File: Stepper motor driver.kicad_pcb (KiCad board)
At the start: 2 copper layers, 16 parts, among them P1 CONN_01X04, P2 CONN_01X04, Q1 TIP120, Q2 TIP120, Q3 TIP120, Q4 TIP120, U1 74LS175, U2 74LS157

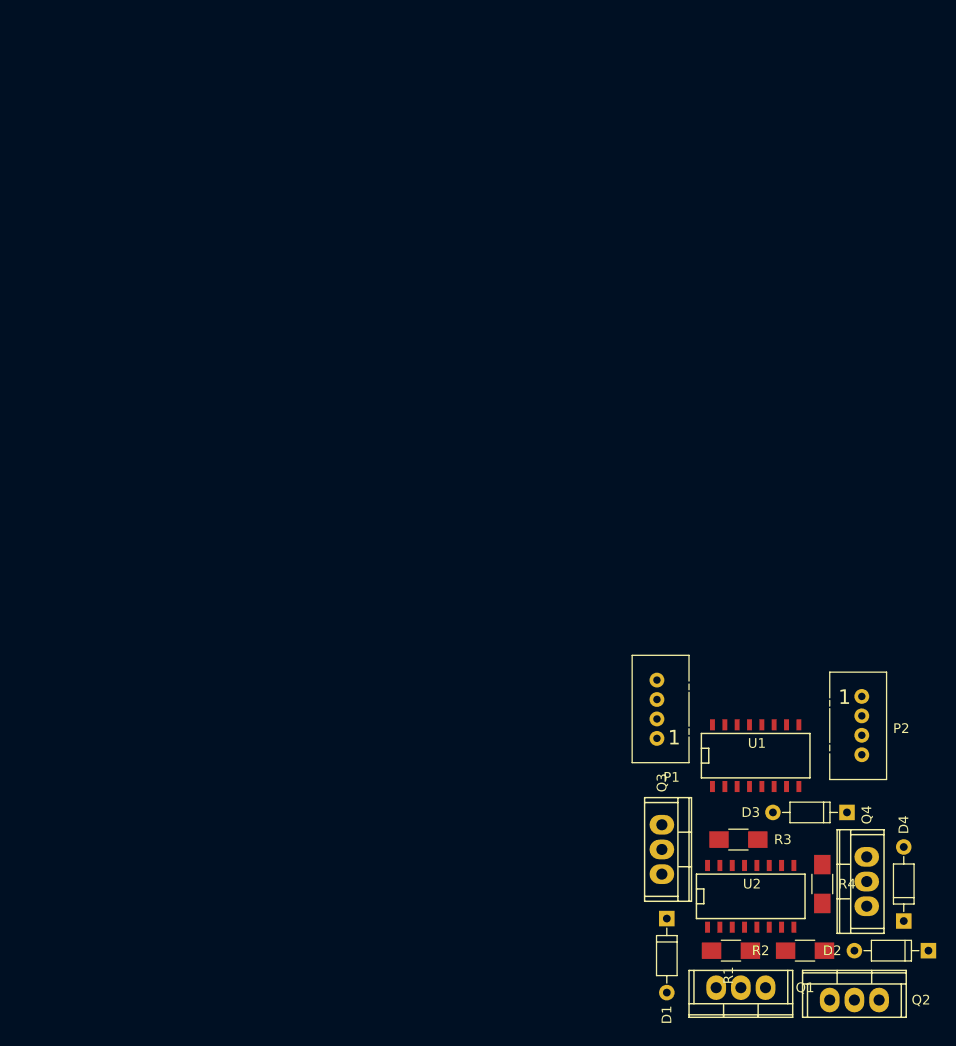
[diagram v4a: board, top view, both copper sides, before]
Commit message: Cleaned up schematic and placed PCB components
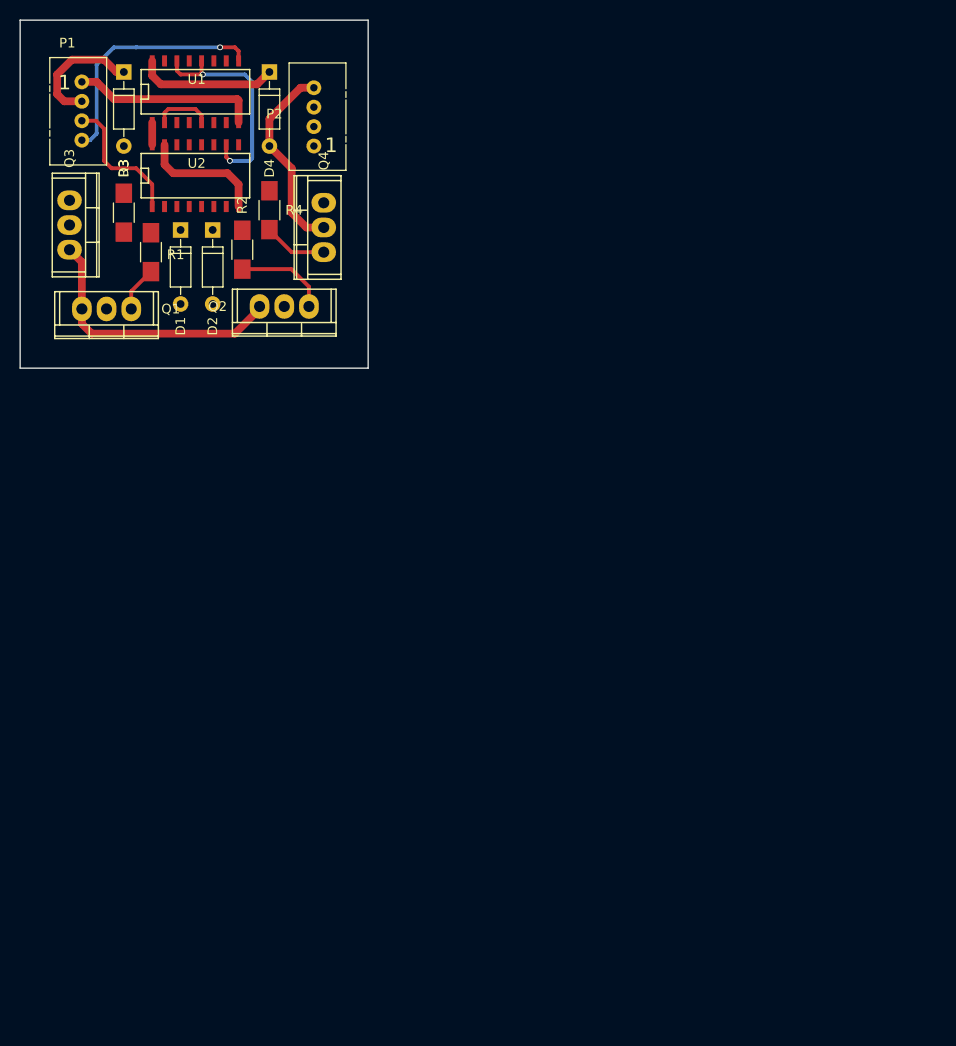
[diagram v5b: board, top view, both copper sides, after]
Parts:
- moved D4 109.1 mm to (144.0, 29.7), turned to 270 degrees
- moved D3 106.5 mm to (129.0, 29.7), turned to 270 degrees
- moved D2 104.5 mm to (138.2, 46.0), turned to 270 degrees
- moved Q1 95.6 mm to (127.3, 54.1)
- moved U2 93.6 mm to (136.4, 40.4)
- moved R1 93.4 mm to (131.8, 48.3), turned to 90 degrees
- moved R2 92.5 mm to (141.2, 48.0), turned to 90 degrees
- moved Q2 92.4 mm to (145.5, 53.8), turned to 180 degrees
- moved R3 90.3 mm to (129.0, 44.2), turned to 90 degrees
- moved P1 89.8 mm to (124.7, 30.7), turned to 0 degrees
- moved R4 89.7 mm to (144.0, 43.9)
- moved U1 89.4 mm to (136.4, 31.8)
- moved Q3 88.6 mm to (123.4, 45.5)
- moved Q4 87.5 mm to (149.6, 45.7)
- moved D1 86.8 mm to (134.9, 46.0)
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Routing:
- net GND: track 0.00 -> 60.1 mm
- net VCC: track 0.00 -> 29.7 mm
- net /CLK: track 0.00 -> 25.4 mm, vias 0 -> 1
- net /B2-: track 0.00 -> 22.8 mm, vias 0 -> 2
- net Net-(D4-Pad2): track 0.00 -> 20.4 mm
- net /DIR: track 0.00 -> 14.2 mm
- net Net-(Q2-Pad1): track 0.00 -> 9.64 mm
- net Net-(Q4-Pad1): track 0.00 -> 6.57 mm
- net /B1+: track 0.00 -> 6.01 mm
- net Net-(Q1-Pad1): track 0.00 -> 4.68 mm
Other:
- board outline added: 35.8 x 35.8 mm

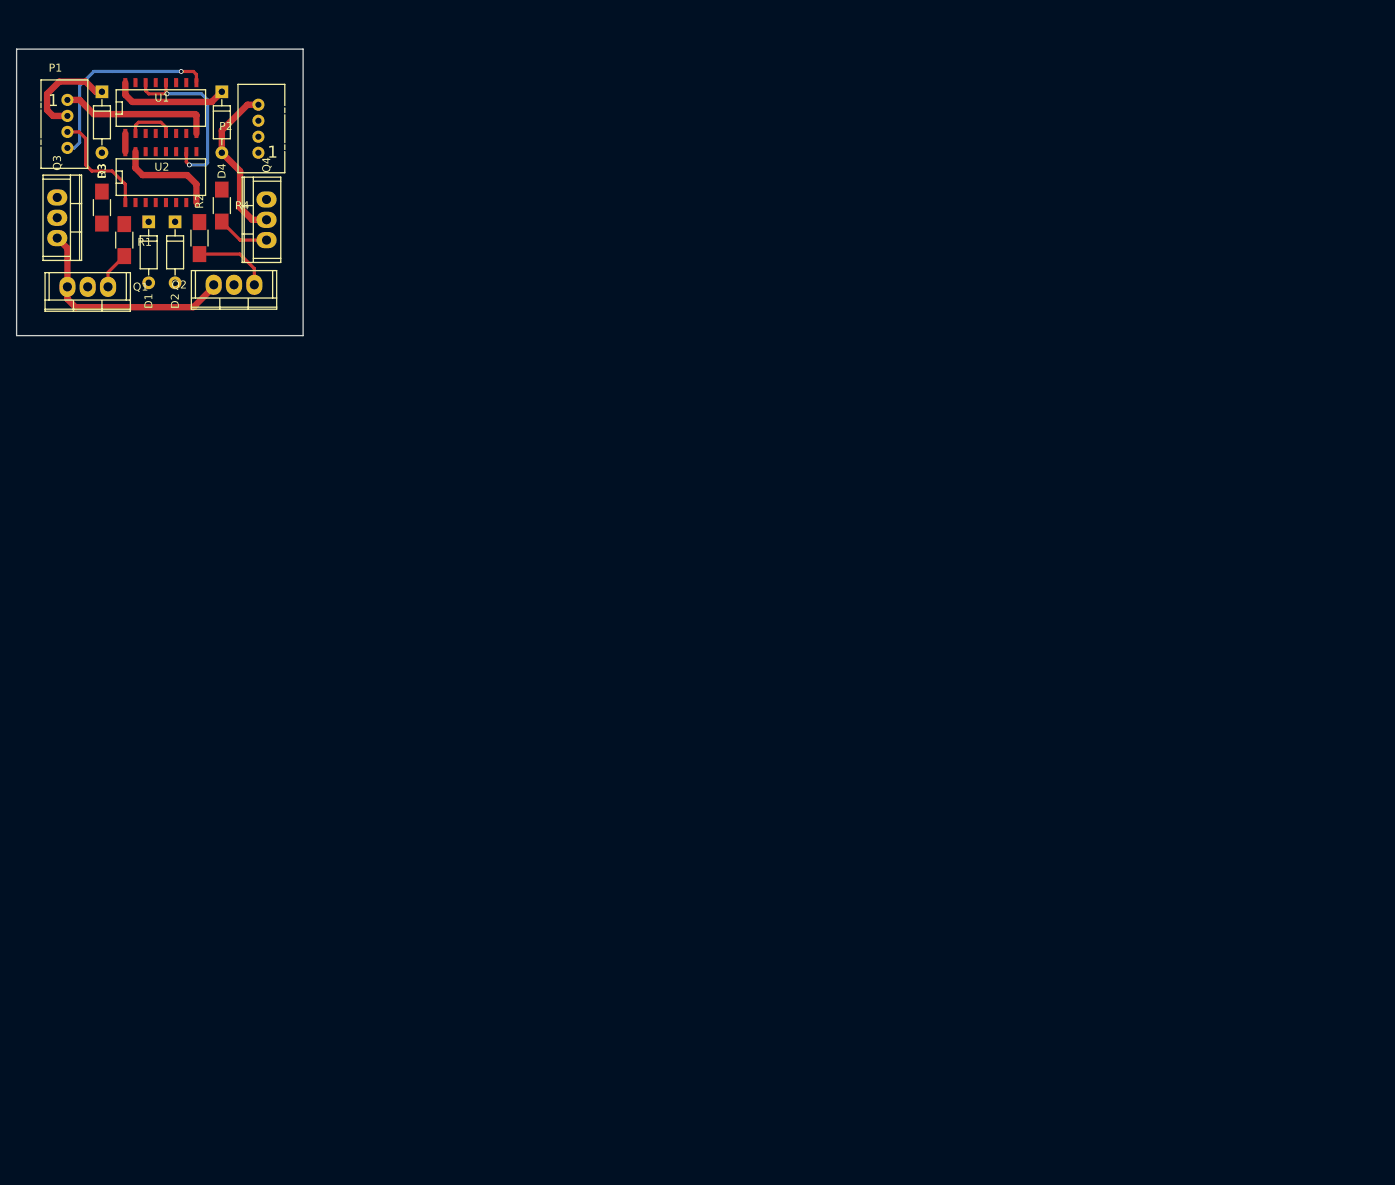
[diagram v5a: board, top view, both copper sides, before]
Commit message: Small schematic change, fine component placement, silkscreen
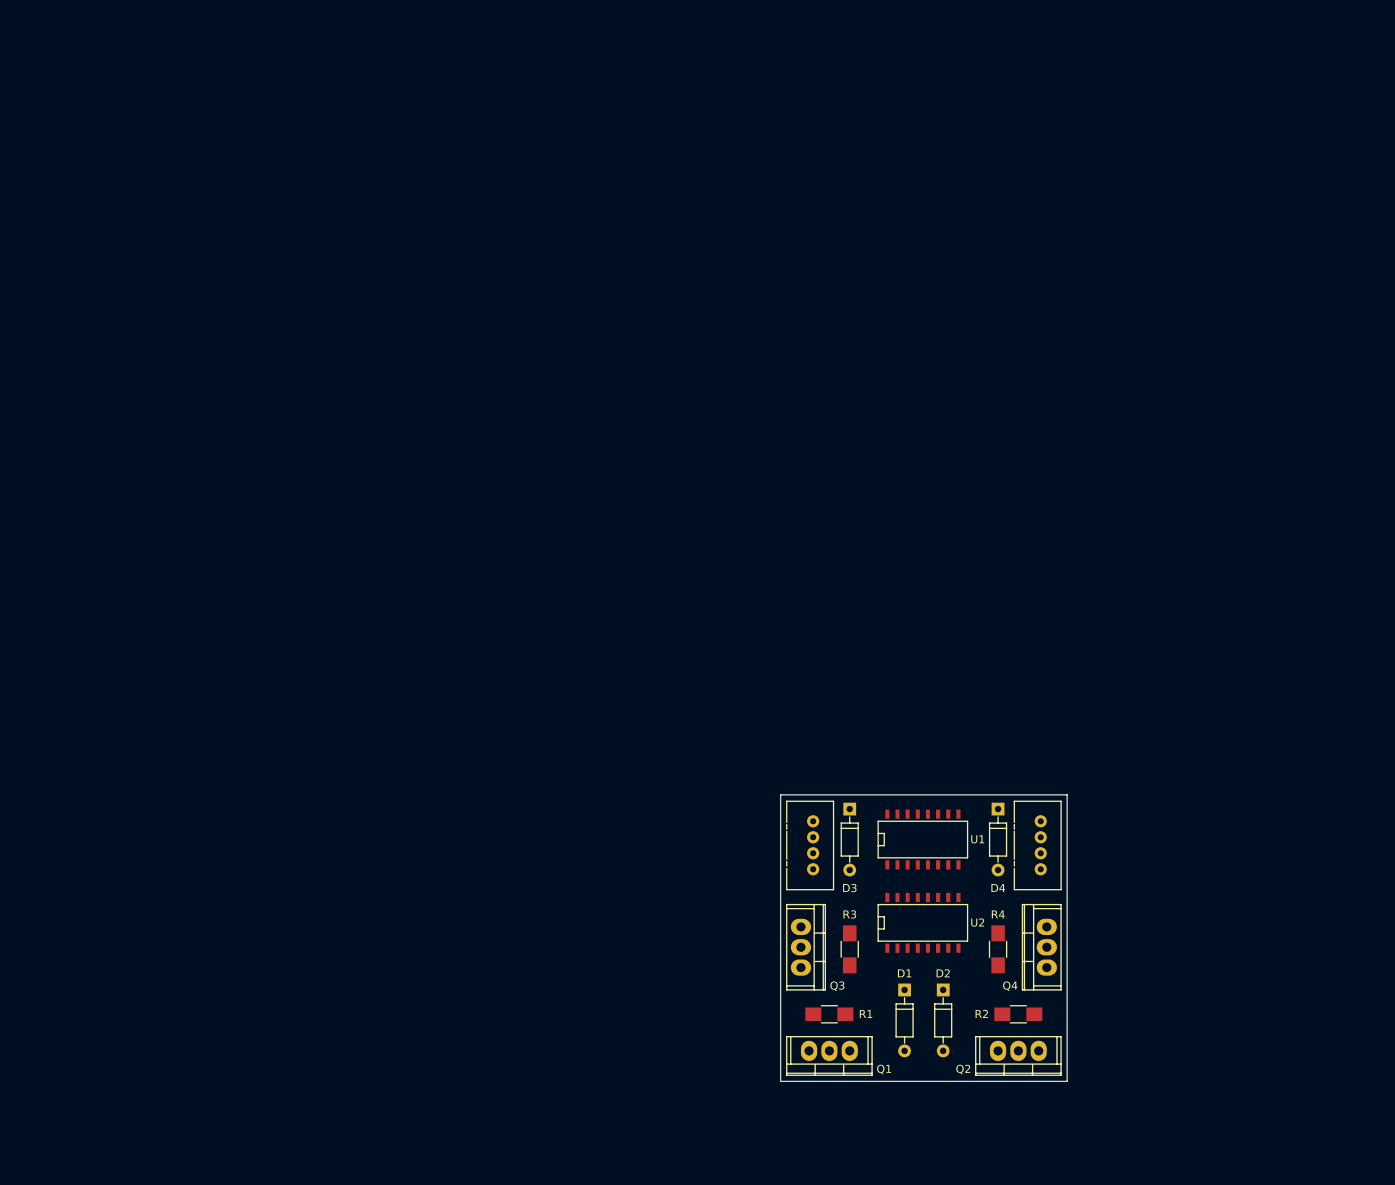
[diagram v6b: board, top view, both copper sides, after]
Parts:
- removed P1, P2: CONN_01X04, Connect:Grove_1x04
- added ?: CONN_01X04, Connect:Grove_1x04, F.Cu at (217.9, 120.9)
- added ?: CONN_01X04, Connect:Grove_1x04, F.Cu at (246.4, 120.9)
- moved R2 141.0 mm to (243.6, 145.0), turned to 180 degrees
- moved Q2 137.0 mm to (243.6, 149.6)
- moved D2 135.8 mm to (234.2, 142.0)
- moved D1 134.7 mm to (229.4, 142.0)
- moved R4 134.4 mm to (241.0, 136.9)
- moved Q4 133.3 mm to (247.1, 136.7)
- moved U2 133.3 mm to (231.6, 133.6)
- moved Q1 133.1 mm to (220.0, 149.6)
- moved D4 132.1 mm to (241.0, 119.4)
- moved U1 132.0 mm to (231.6, 123.2)
- moved R3 131.7 mm to (222.5, 136.9)
- moved R1 130.9 mm to (220.0, 145.0), turned to 0 degrees
- moved Q3 130.2 mm to (216.4, 136.7)
- moved D3 129.5 mm to (222.5, 119.4)
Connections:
- net Net-(D1-Pad2) renamed /Coil1+
- net Net-(D2-Pad2) renamed /Coil1-
- net Net-(D3-Pad2) renamed /Coil2+
- net Net-(D4-Pad2) renamed /Coil2-
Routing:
- net GND: track 60.1 -> 0.00 mm
- net VCC: track 29.7 -> 0.00 mm
- net /CLK: track 25.4 -> 0.00 mm, vias 1 -> 0
- net /B2-: track 22.8 -> 0.00 mm, vias 2 -> 0
- net /Coil2-: track 20.4 -> 0.00 mm
- net /DIR: track 14.2 -> 0.00 mm
- net Net-(Q2-Pad1): track 9.64 -> 0.00 mm
- net Net-(Q4-Pad1): track 6.57 -> 0.00 mm
- net /B1+: track 6.01 -> 0.00 mm
- net Net-(Q1-Pad1): track 4.68 -> 0.00 mm

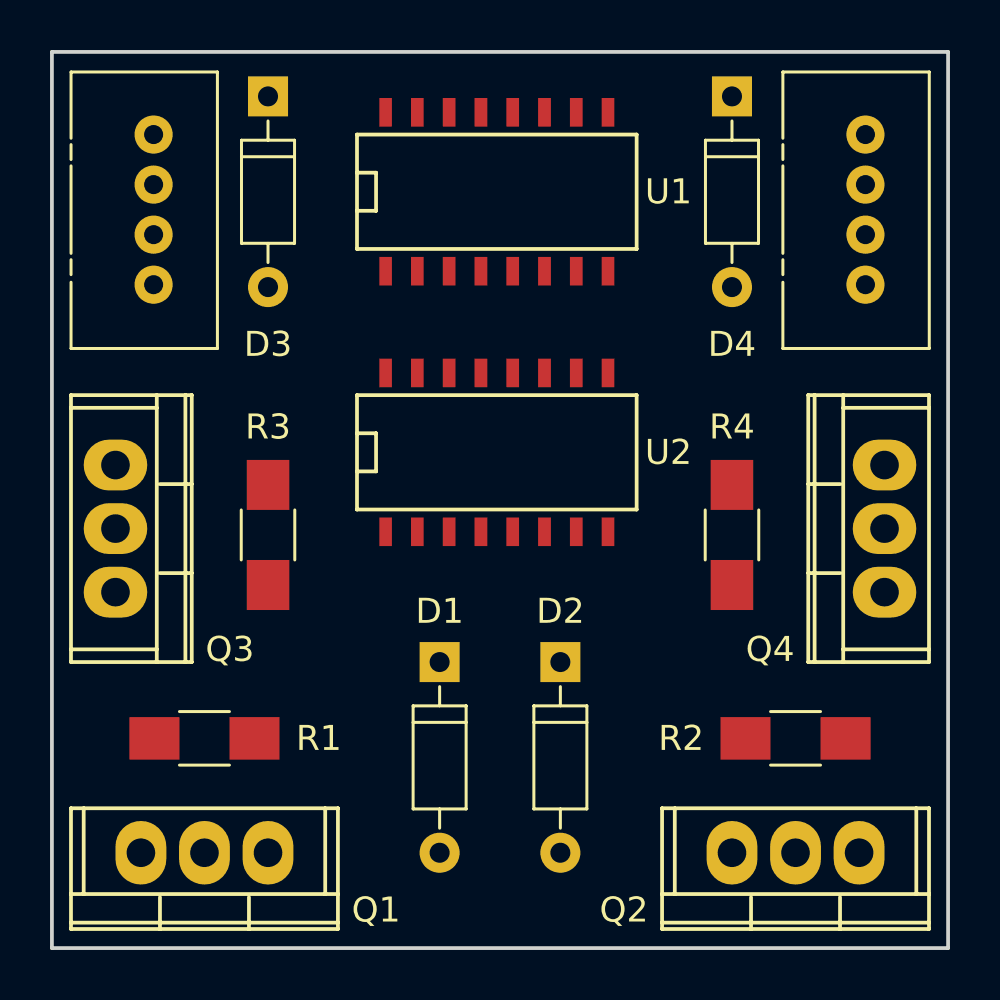
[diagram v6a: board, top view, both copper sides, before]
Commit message: Added VCC to output, initial board routing
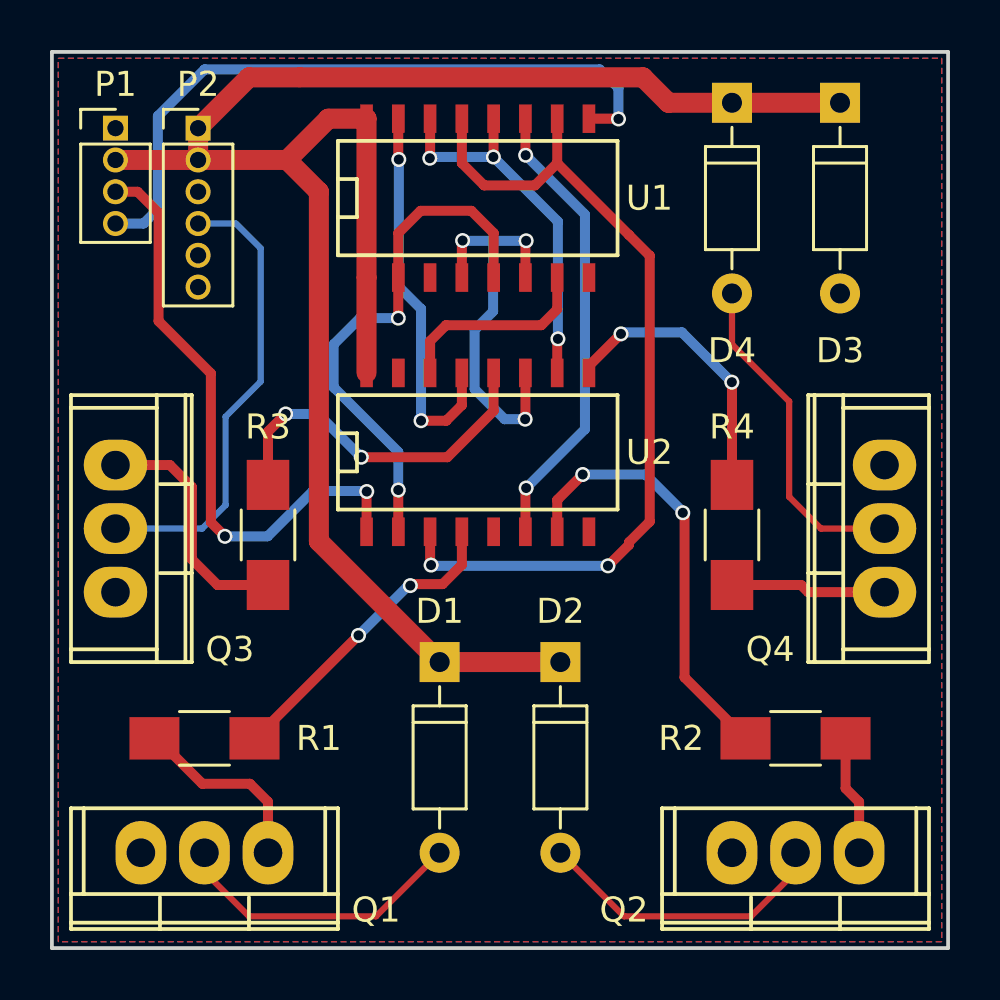
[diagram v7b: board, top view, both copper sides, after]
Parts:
- removed ? (x2): CONN_01X04, Connect:Grove_1x04
- added P1: CONN_01X04, Pin_Headers:Pin_Header_Straight_1x04_Pitch1.27mm, F.Cu at (216.4, 120.7)
- added P2: CONN_01X06, Pin_Headers:Pin_Header_Straight_1x06_Pitch1.27mm, F.Cu at (219.7, 120.7)
- moved D3 22.9 mm to (245.4, 119.6)
- moved U1 0.80 mm to (230.9, 123.4)
- moved U2 0.76 mm to (230.9, 133.6)
- moved D4 0.25 mm to (241.0, 119.6)
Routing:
- net VCC: track 0.00 -> 76.5 mm
- net /A2-: track 0.00 -> 34.8 mm, vias 0 -> 2
- net /CLK: track 0.00 -> 27.6 mm, vias 0 -> 1
- net /DIR: track 0.00 -> 24.1 mm, vias 0 -> 2
- net /B1+: track 0.00 -> 21.3 mm, vias 0 -> 2
- net /Coil2+: track 0.00 -> 18.5 mm
- net /A2+: track 0.00 -> 18.5 mm, vias 0 -> 2
- net Net-(R2-Pad2): track 0.00 -> 17.4 mm, vias 0 -> 2
- net /A1+: track 0.00 -> 16.1 mm, vias 0 -> 3
- net /B2+: track 0.00 -> 15.7 mm, vias 0 -> 2
- net /B2-: track 0.00 -> 15.4 mm, vias 0 -> 3
- net Net-(R3-Pad2): track 0.00 -> 14.4 mm, vias 0 -> 2
- net /Coil2-: track 0.00 -> 13.4 mm
- net Net-(R1-Pad2): track 0.00 -> 12.5 mm, vias 0 -> 2
- net /Coil1-: track 0.00 -> 11.9 mm
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- added copper zone on B.Cu, net GND
- added copper zone on F.Cu, net GND

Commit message: Continued routing progress
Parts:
- moved P2 1.02 mm to (220.7, 120.7)
- moved D3 0.25 mm to (245.6, 119.6)
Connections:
- P1 pad 1: GND -> VCC
- P1 pad 2: VCC -> /CLK
- P1 pad 4: /CLK -> GND
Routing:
- net (no net): track 0.00 -> 71.6 mm
- net /Coil2+: track 18.5 -> 0.00 mm
- net /B1-: track 0.00 -> 12.9 mm, vias 0 -> 2
- net /B2+: track 15.7 -> 21.6 mm
- net /A2-: track 34.8 -> 37.7 mm
- net /B1+: track 21.3 -> 22.9 mm
- net /CLK: track 27.6 -> 28.4 mm
- net VCC: track 76.5 -> 75.7 mm
- net /A1+: track 16.1 -> 16.8 mm
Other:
- board text added: "(P2)"
- board text added: "Add a 3 pin connector for coil 1 here"
- board text added: "Add a 3 pin connector for coil 2 here"
- board text added: "remove this connector"
